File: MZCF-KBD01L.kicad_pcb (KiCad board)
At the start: 2 copper layers, 142.1 x 127.8 mm, 78 parts, among them CN1 XH-4AW_C2908613, SW1 SW_Push, SW10 SW_Push, SW11 SW_Push, SW12 SW_Push, SW13 SW_Push, SW15 SW_Push, SW16 SW_Push, SW17 SW_Push, SW18 SW_Push, SW19 SW_Push, SW2 SW_Push, SW20 SW_Push, SW22 SW_Push, SW23 SW_Push, SW24 SW_Push, SW25 SW_Push, SW26 SW_Push, SW27 SW_Push, SW29 SW_Push, SW3 SW_Push, SW30 SW_Push, SW31 SW_Push, SW32 SW_Push, SW33 SW_Push, SW37 SW_Push, SW38 SW_Push, SW39 SW_Push, SW4 SW_Push, SW40 SW_Push, SW5 SW_Push, SW6 SW_Push, SW8 SW_Push, SW9 SW_Push, U1 RP2040-ZERO

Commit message: feat: new left keyboard
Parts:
- removed D24, D37, D38, D39, D40: 1N4148W, ComboDiode
- removed SW24, SW37, SW38, SW39, SW40: SW_Push, MX
- added D14: 1N4148W, ComboDiode, B.Cu at (74.9, 70.4)
- added D21: 1N4148W, ComboDiode, B.Cu at (103.5, 89.5)
- added D28: 1N4148W, ComboDiode, B.Cu at (127.3, 108.5)
- added D34: 1N4148W, ComboDiode, B.Cu at (146.4, 108.5)
- added D35: 1N4148W, ComboDiode, B.Cu at (155.9, 127.6)
- added H10: MountingHole_2.2mm_M2, MountingHole:MountingHole_2.2mm_M2, F.Cu at (27.9, 150.5)
- added H11: MountingHole_2.2mm_M2, MountingHole:MountingHole_2.2mm_M2, F.Cu at (162.6, 150.5)
- added SW14: SW_Push, MX, F.Cu at (74.9, 65.4)
- added SW21: SW_Push, MX, F.Cu at (103.5, 84.5)
- added SW28: SW_Push, MX, F.Cu at (127.3, 103.5)
- added SW34: SW_Push, MX, F.Cu at (146.4, 103.5)
- added SW35: SW_Push, MX, F.Cu at (155.9, 122.6)
- CN1: value XH-4AW_C2908613 -> PJ-320A_C49284721; footprint lcsc_footprints:C2908613_CONN-TH_XH-4AW -> lcsc_footprints:C49284721_AUDIO-TH_PJ-320A_C49284721
- moved D13 118.6 mm to (74.9, 41.8), turned to 0 degrees
- moved SW13 118.6 mm to (74.9, 36.8)
- moved H5 109.0 mm to (148.6, 51.4)
- moved H1 104.5 mm to (27.9, 27.9)
- moved D19 99.5 mm to (94.0, 41.8), turned to 0 degrees
- moved SW19 99.5 mm to (94.0, 36.8)
- moved CN1 97.0 mm to (142.9, 35.1)
- moved U1 92.9 mm to (55.9, 39.3)
- moved D20 90.0 mm to (94.0, 70.4), turned to 0 degrees
- moved SW20 90.0 mm to (94.0, 65.4)
- moved H9 80.8 mm to (84.3, 141.7)
- moved D25 80.5 mm to (113.0, 41.8), turned to 0 degrees
- moved SW25 80.5 mm to (113.0, 36.8)
- moved D29 73.5 mm to (136.8, 127.6), turned to 0 degrees
- moved SW29 73.5 mm to (136.8, 122.6)
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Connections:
- CN1 pad 2: Net-(U1-GP29) -> Net-(U1-5V)
- CN1 pad 3: Net-(U1-GP28) -> Net-(U1-GP29)
- CN1 pad 4: Net-(U1-GND) -> Net-(U1-GP28)
- D10 pad 1: /ROW2 -> /ROW3
- D11 pad 1: /ROW3 -> /ROW4
- D12 pad 1: /ROW4 -> /ROW5
- D13 pad 1: /ROW5 -> /ROW0
- D15 pad 1: /ROW0 -> /ROW2
- D16 pad 1: /ROW1 -> /ROW3
- D17 pad 1: /ROW2 -> /ROW4
- D18 pad 1: /ROW3 -> /ROW5
- D19 pad 1: /ROW4 -> /ROW0
- D20 pad 1: /ROW5 -> /ROW1
- D22 pad 1: /ROW0 -> /ROW3
- D23 pad 1: /ROW1 -> /ROW4
- D25 pad 1: /ROW3 -> /ROW0
- D26 pad 1: /ROW4 -> /ROW1
- D27 pad 1: /ROW5 -> /ROW2
- D29 pad 1: /ROW0 -> /ROW4
- D30 pad 1: /ROW1 -> /ROW5
- D31 pad 1: /ROW2 -> /ROW0
- D32 pad 1: /ROW3 -> /ROW1
- D33 pad 1: /ROW4 -> /ROW2
- D8 pad 1: /ROW0 -> /ROW1
- D9 pad 1: /ROW1 -> /ROW2
- SW13 pad 1: /COL1 -> /COL2
- SW19 pad 1: /COL2 -> /COL3
- SW20 pad 1: /COL2 -> /COL3
- SW25 pad 1: /COL3 -> /COL4
- SW26 pad 1: /COL3 -> /COL4
- SW27 pad 1: /COL3 -> /COL4
- SW31 pad 1: /COL4 -> /COL5
- SW32 pad 1: /COL4 -> /COL5
- SW33 pad 1: /COL4 -> /COL5
- U1 pad 10: /ROW1 -> /ROW0
- U1 pad 11: /ROW2 -> /ROW1
- U1 pad 12: /ROW3 -> /ROW2
- U1 pad 13: /ROW4 -> /ROW3
- U1 pad 14: /ROW5 -> /ROW4
- U1 pad 15: /ROW6 -> /ROW5
- U1 pad 17: unconnected-(U1-GP26-Pad17) -> Net-(U1-GP26)
- U1 pad 18: unconnected-(U1-GP27-Pad18) -> Net-(U1-GP27)
- U1 pad 9: /ROW0 -> /BTN1
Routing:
- net /COL5: track 89.6 -> 199.1 mm, vias 0 -> 1
- net /COL0: track 226.6 -> 130.2 mm
- net /COL4: track 120.0 -> 198.1 mm, vias 0 -> 1
- net /COL1: track 205.0 -> 137.0 mm
- net Net-(U1-GP28): track 130.2 -> 88.1 mm, vias 2 -> 0
- net /ROW4: track 221.4 -> 262.1 mm
- net Net-(U1-GND): track 116.5 -> 79.3 mm, vias 1 -> 0
- net Net-(U1-GP29): track 116.7 -> 85.0 mm, vias 2 -> 0
- net /ROW3: track 198.1 -> 229.1 mm
- net /COL2: track 180.2 -> 153.7 mm, vias 0 -> 1
- net /ROW2: track 177.7 -> 201.0 mm
- net Net-(U1-5V): track 112.7 -> 93.6 mm, vias 1 -> 0
- net Net-(D34-A): track 0.00 -> 16.3 mm
- net Net-(D28-A): track 0.00 -> 16.3 mm
- net Net-(D21-A): track 0.00 -> 16.3 mm
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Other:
- board size 142.1 x 127.8 mm -> 140.1 x 127.8 mm
- board text added: "MZCF-KBD01R V1 Rev.2"
- board text removed: "MZCF-KBD01L V1 Rev.1"

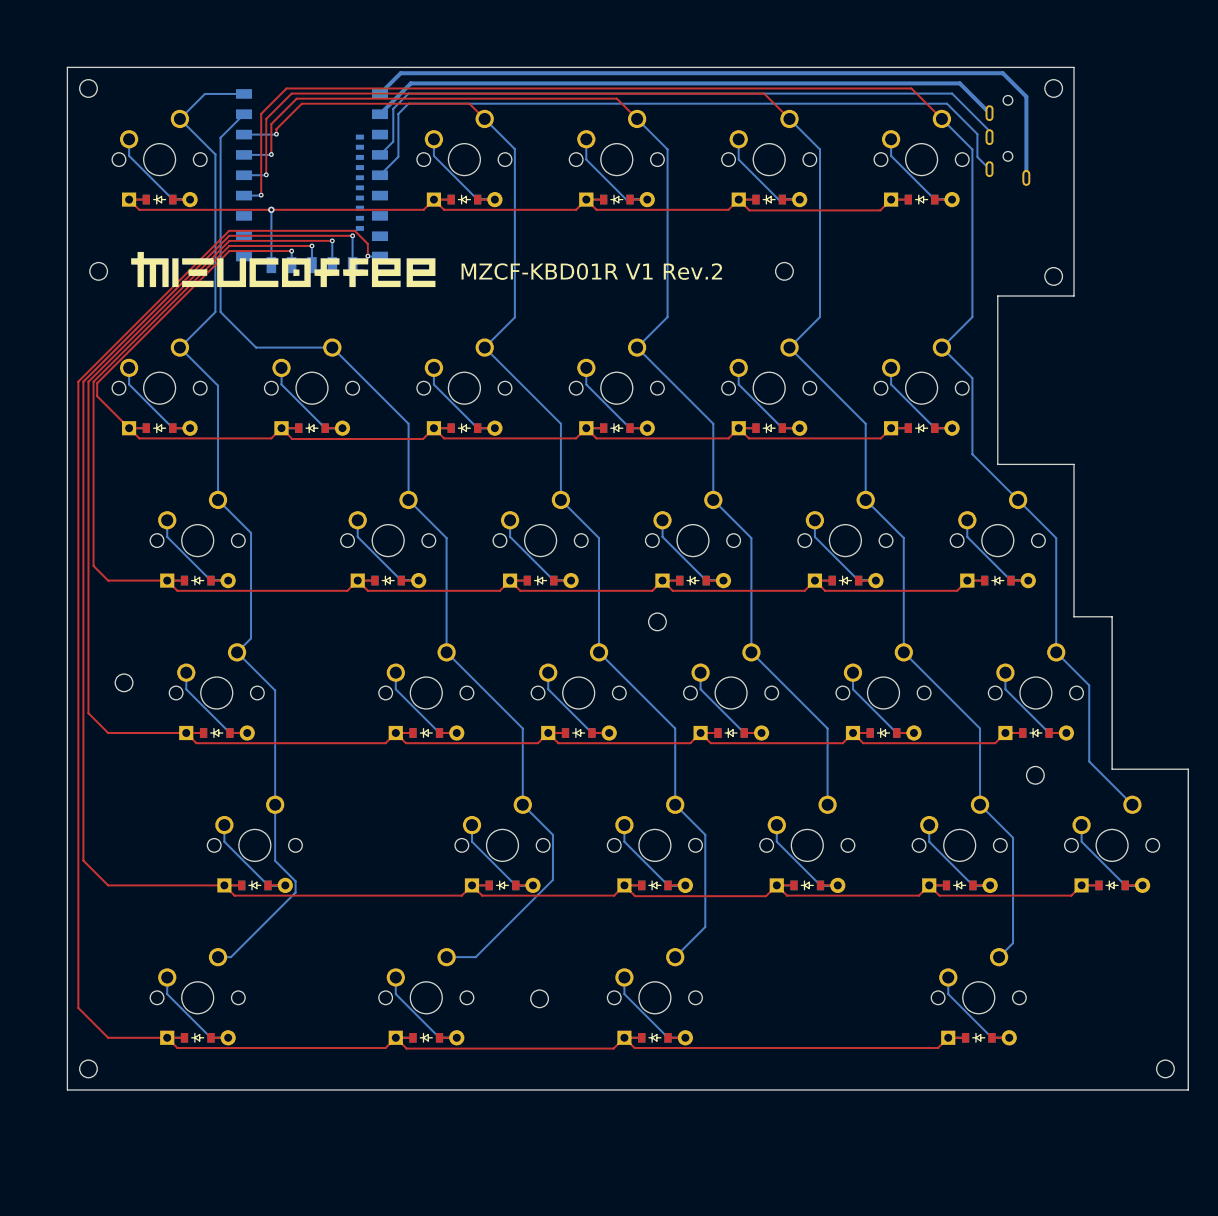
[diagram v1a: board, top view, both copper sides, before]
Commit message: feat: add hotswap MX switches and PCB stabilizer support
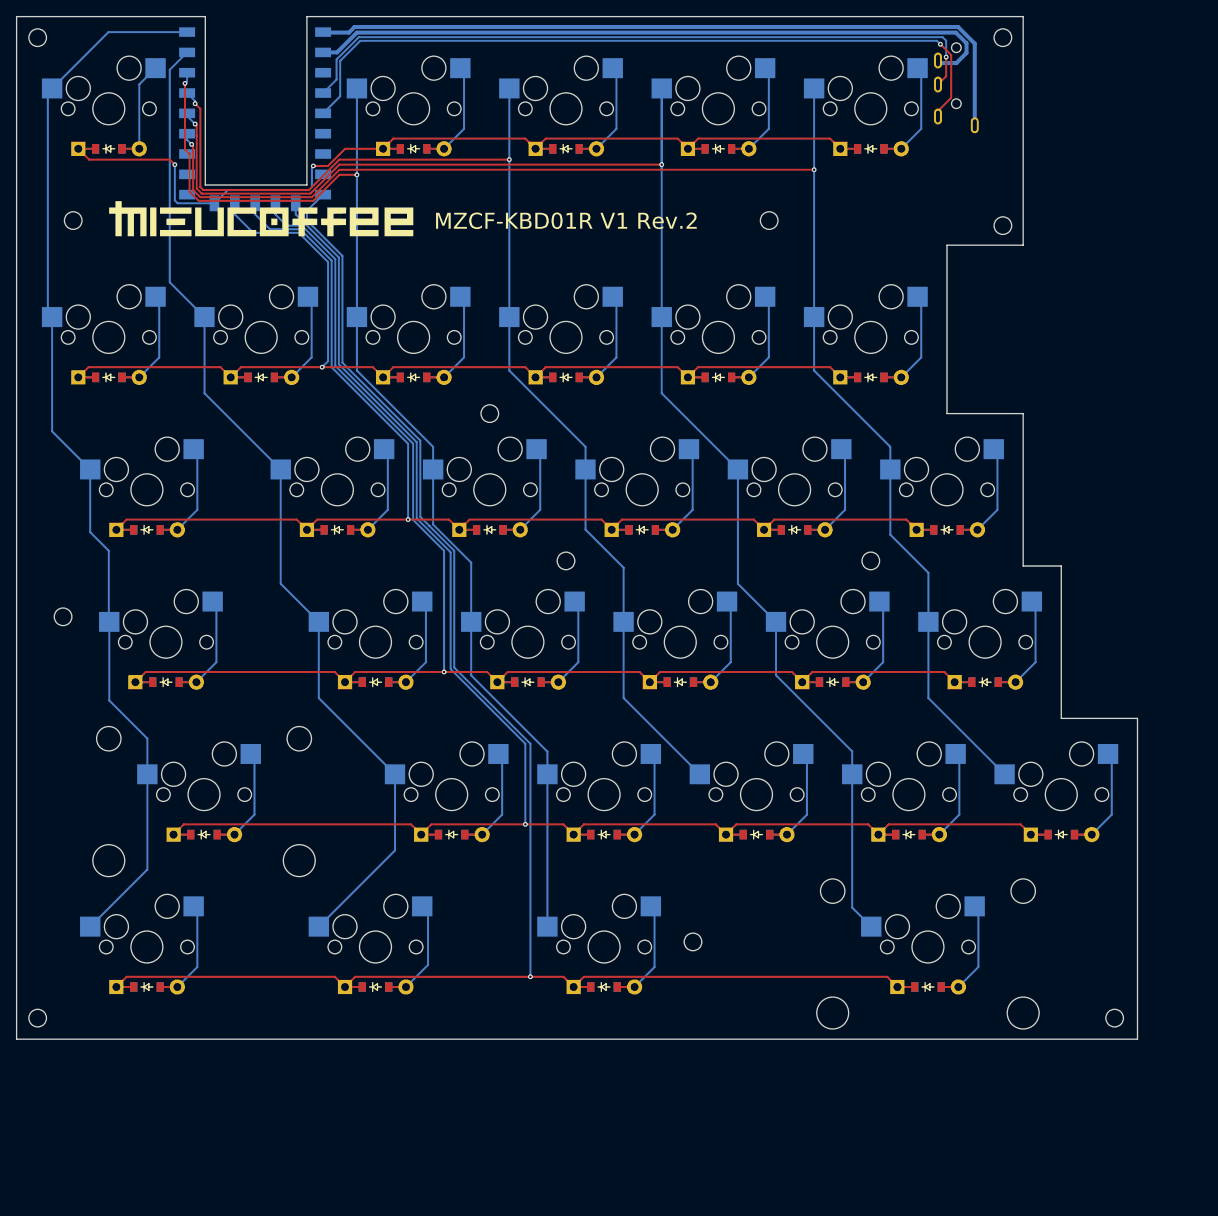
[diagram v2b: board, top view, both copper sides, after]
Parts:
- removed the H1 at (27.9, 27.9)
- removed H10, H11, H2, H3, H4, H5, H6, H7, H8, H9: MountingHole_2.2mm_M2, MountingHole:MountingHole_2.2mm_M2
- added H1: MountingHole_2.2mm_M2, MountingHole:MountingHole_2.2mm_M2, F.Cu at (78.1, 68.6)
- added H1: MountingHole_2.2mm_M2, MountingHole:MountingHole_2.2mm_M2, F.Cu at (125.7, 87.0)
- added H1: MountingHole_2.2mm_M2, MountingHole:MountingHole_2.2mm_M2, F.Cu at (21.6, 144.1)
- added H1: MountingHole_2.2mm_M2, MountingHole:MountingHole_2.2mm_M2, F.Cu at (156.2, 144.1)
- added H1: MountingHole_2.2mm_M2, MountingHole:MountingHole_2.2mm_M2, F.Cu at (142.2, 21.6)
- added H1: MountingHole_2.2mm_M2, MountingHole:MountingHole_2.2mm_M2, F.Cu at (26.0, 44.5)
- added H1: MountingHole_2.2mm_M2, MountingHole:MountingHole_2.2mm_M2, F.Cu at (103.5, 134.6)
- added H1: MountingHole_2.2mm_M2, MountingHole:MountingHole_2.2mm_M2, F.Cu at (24.8, 94.0)
- added H1: MountingHole_2.2mm_M2, MountingHole:MountingHole_2.2mm_M2, F.Cu at (142.2, 45.1)
- added H1: MountingHole_2.2mm_M2, MountingHole:MountingHole_2.2mm_M2, F.Cu at (113.0, 44.5)
- added H1: MountingHole_2.2mm_M2, MountingHole:MountingHole_2.2mm_M2, F.Cu at (21.6, 21.6)
- added H1: MountingHole_2.2mm_M2, MountingHole:MountingHole_2.2mm_M2, F.Cu at (87.6, 87.0)
- added ST1: , STAB_MX, F.Cu at (42.4, 116.2)
- added ST2: , STAB_MX, F.Cu at (132.9, 135.3)
- moved U1 10.5 mm to (48.8, 31.6)
- moved CN1 9.21 mm to (136.4, 28.5)
- moved D35 8.98 mm to (149.5, 121.2)
- moved SW35 8.98 mm to (149.5, 116.2)
- moved D17 8.98 mm to (92.4, 121.2)
- moved D23 8.98 mm to (111.4, 121.2)
- moved SW17 8.98 mm to (92.4, 116.2)
- moved SW23 8.98 mm to (111.4, 116.2)
- moved D13 8.98 mm to (68.6, 35.5)
- moved D19 8.98 mm to (87.6, 35.5)
- moved D31 8.98 mm to (125.7, 35.5)
- moved D5 8.98 mm to (42.4, 121.2)
- moved SW14 8.98 mm to (68.6, 59.1)
- moved SW20 8.98 mm to (87.6, 59.1)
- moved SW32 8.98 mm to (125.7, 59.1)
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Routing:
- net /ROW4: track 262.1 -> 227.9 mm
- net /ROW5: track 256.8 -> 228.3 mm
- net /ROW3: track 229.1 -> 202.0 mm
- net /ROW2: track 201.0 -> 180.9 mm
- net /COL5: track 199.1 -> 182.4 mm, vias 1 -> 2
- net /ROW1: track 166.7 -> 155.4 mm
- net /COL1: track 137.0 -> 125.8 mm
- net Net-(U1-GND): track 79.3 -> 87.4 mm, vias 0 -> 1
- net Net-(U1-GP28): track 88.1 -> 94.0 mm, vias 0 -> 1
- net /COL3: track 154.1 -> 149.0 mm, vias 1 -> 2
- net Net-(U1-GP29): track 85.0 -> 88.3 mm, vias 0 -> 1
- net /COL0: track 130.2 -> 132.9 mm
- net /ROW0: track 128.1 -> 129.7 mm, vias 1 -> 2
- net /COL4: track 198.1 -> 196.5 mm, vias 1 -> 2
- net /COL2: track 153.7 -> 152.6 mm, vias 1 -> 2
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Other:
- outline, holes or cut-outs redrawn

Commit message: fix(pcb): add controller cutouts and mating-edge clearance
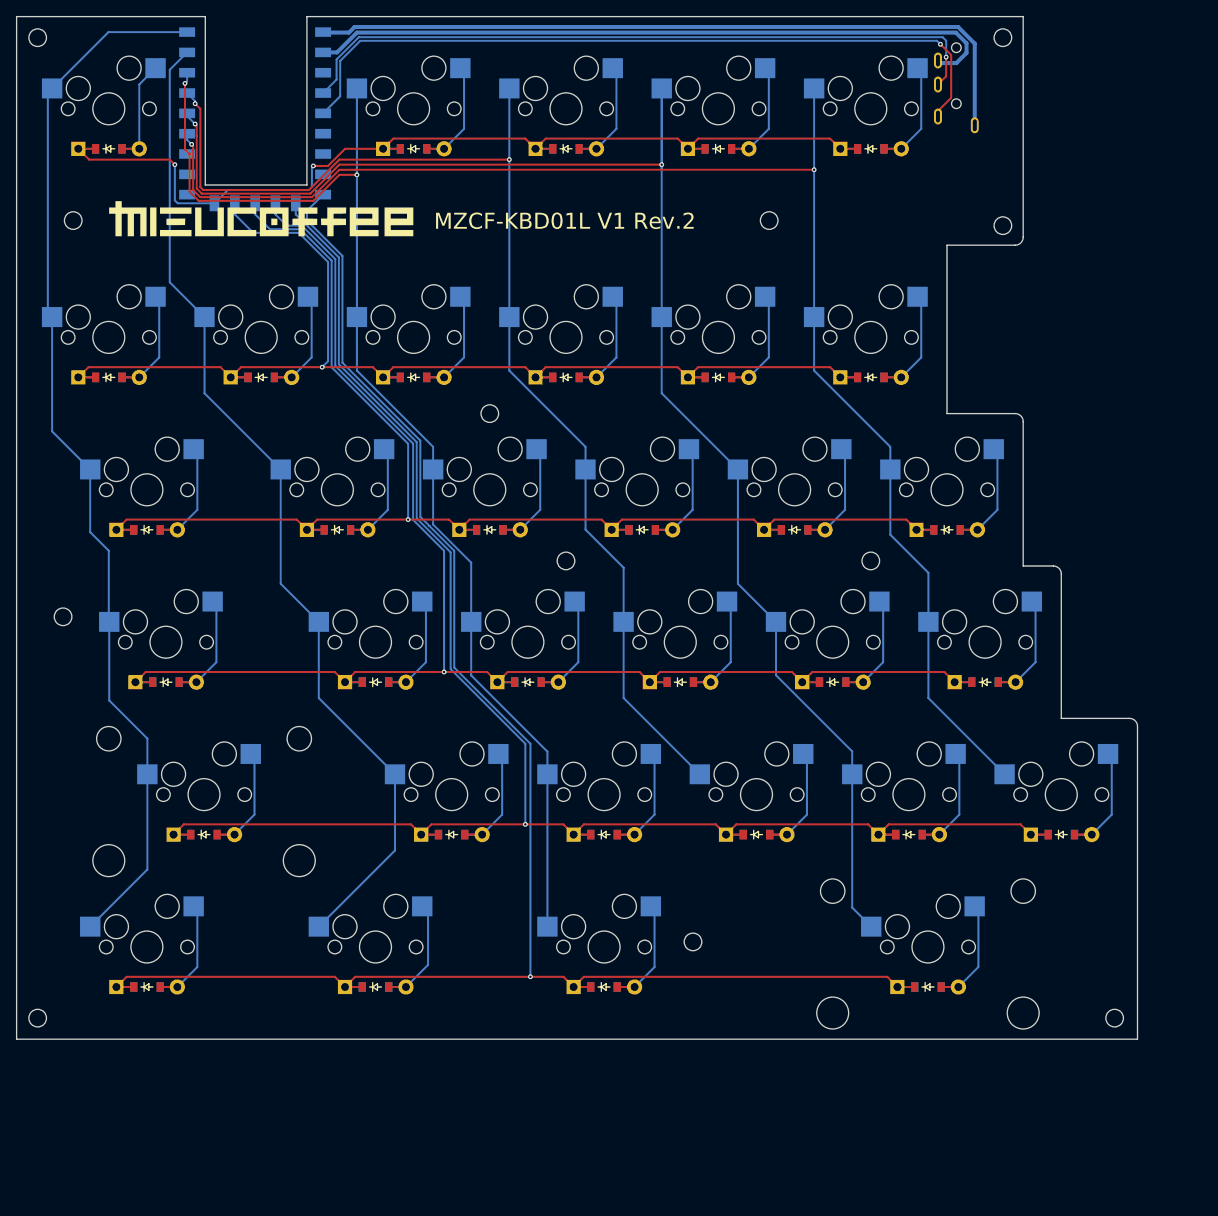
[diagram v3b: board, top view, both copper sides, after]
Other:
- outline, holes or cut-outs redrawn
- board text added: "MZCF-KBD01L V1 Rev.2"
- board text removed: "MZCF-KBD01R V1 Rev.2"
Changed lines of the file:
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@@
 	(gr_line
 		(start 135.255 47.53)
-		(end 144.78 47.53)
+		(end 143.78 47.53)
 		(stroke
 			(width 0.15)
@@
 	)
 	(gr_line
-		(start 144.78 47.53)
+		(start 143.78 68.58)
+		(end 135.255 68.58)
+		(stroke
+			(width 0.15)
+			(type solid)
+		)
+		(layer "Edge.Cuts")
+	)
+	(gr_arc
+		(start 143.78 68.58)
+		(mid 144.487107 68.872893)
+		(end 144.78 69.58)
+		(stroke
+			(width 0.15)
+			(type default)
+		)
+		(layer "Edge.Cuts")
+	)
+	(gr_arc
+		(start 144.78 46.53)
+		(mid 144.487107 47.237107)
+		(end 143.78 47.53)
+		(stroke
+			(width 0.15)
+			(type default)
+		)
+		(layer "Edge.Cuts")
+	)
+	(gr_line
+		(start 144.78 46.53)
 		(end 144.78 18.955)
 		(stroke
@@
 	)
 	(gr_line
-		(start 144.78 68.58)
-		(end 135.255 68.58)
+		(start 144.78 87.63)
+		(end 144.78 69.58)
 		(stroke
 			(width 0.15)
@@
 	)
 	(gr_line
-		(start 144.78 87.63)
-		(end 144.78 68.58)
+		(start 148.5425 87.63)
+		(end 144.78 87.63)
+		(stroke
+			(width 0.15)
+			(type solid)
+		)
+		(layer "Edge.Cuts")
+	)
+	(gr_arc
+		(start 148.5425 87.63)
+		(mid 149.249607 87.922893)
+		(end 149.5425 88.63)
+		(stroke
+			(width 0.15)
+			(type default)
+		)
+		(layer "Edge.Cuts")
+	)
+	(gr_line
+		(start 149.5425 106.68)
+		(end 149.5425 88.63)
 		(stroke
 			(width 0.15)
@@
 	)
 	(gr_line
-		(start 149.5425 87.63)
-		(end 144.78 87.63)
-		(stroke
-			(width 0.15)
-			(type solid)
-		)
-		(layer "Edge.Cuts")
-	)
-	(gr_line
-		(start 149.5425 106.68)
-		(end 149.5425 87.63)
-		(stroke
-			(width 0.15)
-			(type solid)
-		)
-		(layer "Edge.Cuts")
-	)
-	(gr_line
-		(start 159.0675 106.68)
+		(start 158.0675 106.68)
 		(end 149.5425 106.68)
 		(stroke
@@
 		(layer "Edge.Cuts")
 	)
+	(gr_arc
+		(start 158.0675 106.68)
+		(mid 158.774607 106.972893)
+		(end 159.0675 107.68)
+		(stroke
+			(width 0.15)
+			(type default)
+		)
+		(layer "Edge.Cuts")
+	)
 	(gr_line
 		(start 159.0675 146.78)
-		(end 159.0675 106.68)
+		(end 159.0675 107.68)
 		(stroke
 			(width 0.15)
@@
 		(layer "Edge.Cuts")
 	)
-	(gr_text "MZCF-KBD01R V1 Rev.2\n"
+	(gr_text "MZCF-KBD01L V1 Rev.2"
 		(at 71.12 45.72 0)
 		(layer "F.SilkS")
